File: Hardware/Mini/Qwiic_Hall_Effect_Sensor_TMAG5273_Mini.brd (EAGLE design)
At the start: 25.4 x 12.7 mm, 38 parts, among them J1 Vertical Qwiic Connector, J2 Vertical Qwiic Connector, Q1 20V/4.2A/52mΩ/1.4W, U1 TMAG5273

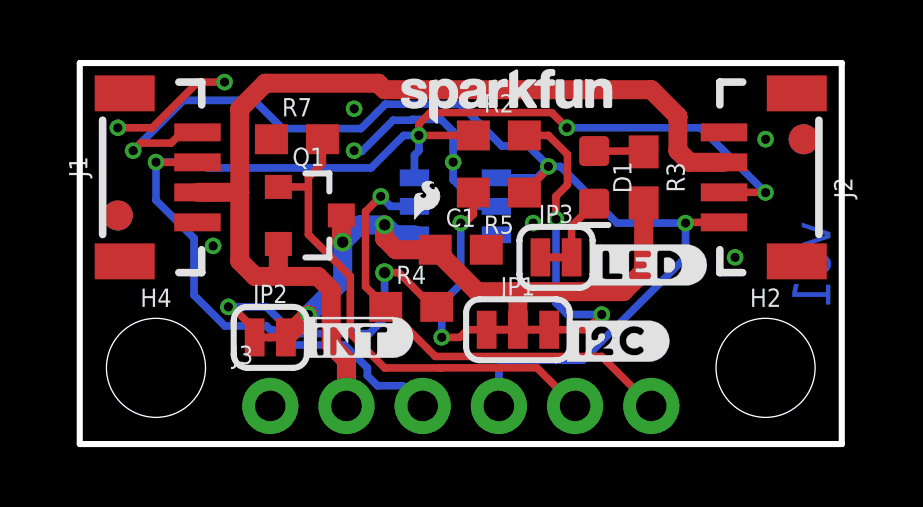
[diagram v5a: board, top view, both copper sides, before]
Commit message: Design review updates
Addition of gerber files for both mini and 1x1, adjusted board for reds engineering checklist run.
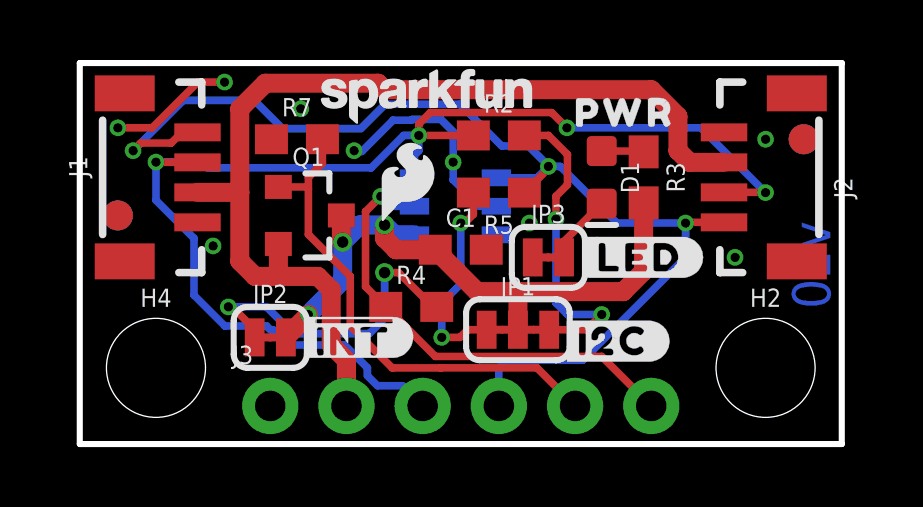
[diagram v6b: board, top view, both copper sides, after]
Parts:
- added U$1: (no value), output:PWR5282
- LOGO6: value SFE_LOGO_FLAME0.05_INCH -> SFE_LOGO_FLAME.1_INCH; device SparkFun-Aesthetics:SFE_LOGO_FLAME_.05 -> SparkFun-Aesthetics:SFE_LOGO_FLAME_.1
- moved LOGO4 2.67 mm to (11.6, 11.7)
- moved LOGO6 0.90 mm to (10.9, 8.76)
- moved U$10 0.28 mm to (18.7, 6.22)
- moved D1 0.25 mm to (17.4, 8.89)
- moved JP3 0.25 mm to (15.6, 6.22)
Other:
- board text added: "v10"
- board text removed: "v01"
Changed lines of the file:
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@@
 <layer number="37" name="tTest" color="7" fill="1" visible="no" active="yes"/>
 <layer number="38" name="bTest" color="7" fill="1" visible="no" active="yes"/>
-<layer number="39" name="tKeepout" color="4" fill="11" visible="no" active="yes"/>
-<layer number="40" name="bKeepout" color="1" fill="11" visible="no" active="yes"/>
-<layer number="41" name="tRestrict" color="4" fill="10" visible="no" active="yes"/>
-<layer number="42" name="bRestrict" color="1" fill="10" visible="no" active="yes"/>
+<layer number="39" name="tKeepout" color="4" fill="11" visible="yes" active="yes"/>
+<layer number="40" name="bKeepout" color="1" fill="11" visible="yes" active="yes"/>
+<layer number="41" name="tRestrict" color="4" fill="10" visible="yes" active="yes"/>
+<layer number="42" name="bRestrict" color="1" fill="10" visible="yes" active="yes"/>
 <layer number="43" name="vRestrict" color="2" fill="10" visible="no" active="yes"/>
 <layer number="44" name="Drills" color="7" fill="1" visible="no" active="yes"/>
 <layer number="45" name="Holes" color="7" fill="1" visible="yes" active="yes"/>
-<layer number="46" name="Milling" color="3" fill="1" visible="yes" active="yes"/>
+<layer number="46" name="Milling" color="3" fill="1" visible="no" active="yes"/>
 <layer number="47" name="Measures" color="7" fill="1" visible="no" active="yes"/>
 <layer number="48" name="Document" color="7" fill="1" visible="no" active="yes"/>
@@
 <dimension x1="4.699" y1="8.89" x2="0" y2="8.89" x3="2.3495" y3="19.05" textsize="1.778" layer="47" unit="inch"/>
 <dimension x1="2.54" y1="2.54" x2="0" y2="2.54" x3="1.27" y3="22.86" textsize="1.778" layer="47" unit="inch"/>
-<text x="24.384" y="5.969" size="1.27" layer="16" font="vector" ratio="15" rot="SMR270" align="center">v01</text>
+<text x="24.384" y="5.969" size="1.27" layer="16" font="vector" ratio="15" rot="SMR270" align="center">v10</text>
 </plain>
 <attributes>
@@
 <element name="FRAME1" library="SparkFun-Aesthetics" package="CREATIVE_COMMONS" value="FRAME-LETTER" x="-11.43" y="-24.13" smashed="yes">
 <attribute name="DESIGNER" value="M. Chodikov" x="68.58" y="-78.74" size="1.778" layer="27" display="off"/>
-<attribute name="REV" value="v01" x="68.58" y="-78.74" size="1.778" layer="27" display="off"/>
+<attribute name="REV" value="v10" x="68.58" y="-78.74" size="1.778" layer="27" display="off"/>
 </element>
 <element name="H2" library="SparkFun-Hardware" package="STAND-OFF" value="STAND-OFF" x="22.86" y="2.54" smashed="yes">
@@
 <attribute name="VALUE" x="6.35" y="2.413" size="0.6096" layer="27" font="vector" ratio="20" align="top-center"/>
 </element>
-<element name="JP3" library="SparkFun-Jumpers" package="SMT-JUMPER_2_NC_TRACE_SILK" package3d_urn="urn:adsk.eagle:package:39281/1" value="JUMPER-SMT_2_NC_TRACE_SILK" x="15.875" y="6.223" smashed="yes">
-<attribute name="NAME" x="15.875" y="7.366" size="0.6096" layer="25" font="vector" ratio="20" align="bottom-center"/>
-<attribute name="VALUE" x="15.875" y="5.08" size="0.6096" layer="27" font="vector" ratio="20" align="top-center"/>
+<element name="JP3" library="SparkFun-Jumpers" package="SMT-JUMPER_2_NC_TRACE_SILK" package3d_urn="urn:adsk.eagle:package:39281/1" value="JUMPER-SMT_2_NC_TRACE_SILK" x="15.621" y="6.223" smashed="yes">
+<attribute name="NAME" x="15.621" y="7.366" size="0.6096" layer="25" font="vector" ratio="20" align="bottom-center"/>
+<attribute name="VALUE" x="15.621" y="5.08" size="0.6096" layer="27" font="vector" ratio="20" align="top-center"/>
 </element>
 <element name="LOGO1" library="SparkFun-Aesthetics" package="OSHW-LOGO-MINI" value="OSHW-LOGOMINI" x="2.54" y="6.35" smashed="yes" rot="MR0"/>
 <element name="LOGO2" library="SparkFun-Aesthetics" package="SFE_LOGO_NAME_FLAME_5MM" value="SFE_LOGO_NAME_FLAME5_MM" x="6.35" y="8.89" smashed="yes" rot="MR0"/>
 <element name="LOGO3" library="SparkFun-Aesthetics" package="QWIIC_4MM" value="QWIIC_LOGO_4MM" x="22.86" y="7.366" smashed="yes" rot="MR0"/>
-<element name="LOGO4" library="SparkFun-Aesthetics" package="SFE_LOGO_NAME_7MM" value="SFE_LOGO_NAME7_MM" x="14.224" y="11.684" smashed="yes"/>
+<element name="LOGO4" library="SparkFun-Aesthetics" package="SFE_LOGO_NAME_7MM" value="SFE_LOGO_NAME7_MM" x="11.557" y="11.684" smashed="yes"/>
 <element name="LOGO5" library="SparkFun-Aesthetics" package="ORDERING_INSTRUCTIONS" value="SPECIAL_INSTRUCTIONS-ORDERING" x="44.45" y="50.8" smashed="yes"/>
-<element name="LOGO6" library="SparkFun-Aesthetics" package="SFE_LOGO_FLAME_.05" value="SFE_LOGO_FLAME0.05_INCH" x="11.557" y="8.128" smashed="yes"/>
+<element name="LOGO6" library="SparkFun-Aesthetics" package="SFE_LOGO_FLAME_.1" value="SFE_LOGO_FLAME.1_INCH" x="10.922" y="8.763" smashed="yes"/>
 <element name="R2" library="SparkFun-Resistors" package="0603" value="2.2k" x="13.97" y="10.287" smashed="yes">
 <attribute name="NAME" x="13.97" y="11.049" size="0.6096" layer="25" font="vector" ratio="20" align="bottom-center"/>
@@
 <attribute name="VALUE" x="5.08" y="-0.762" size="0.6096" layer="27" font="vector" ratio="20"/>
 </element>
-<element name="U$10" library="output" package="#LED#5275" value="" x="18.796" y="5.969" smashed="yes"/>
-<element name="D1" library="SparkFun-LED" package="LED-0603" value="Red" x="17.145" y="8.89" smashed="yes" rot="R270">
-<attribute name="NAME" x="17.78" y="8.89" size="0.6096" layer="25" font="vector" ratio="20" rot="R270" align="bottom-center"/>
-<attribute name="PROD_ID" value="DIO-17976" x="17.145" y="8.89" size="1.778" layer="27" font="vector" rot="R270" display="off"/>
-<attribute name="VALUE" x="16.51" y="8.89" size="0.6096" layer="27" font="vector" ratio="20" rot="R270" align="top-center"/>
+<element name="U$10" library="output" package="#LED#5275" value="" x="18.669" y="6.223" smashed="yes"/>
+<element name="D1" library="SparkFun-LED" package="LED-0603" value="Red" x="17.399" y="8.89" smashed="yes" rot="R270">
+<attribute name="NAME" x="18.034" y="8.89" size="0.6096" layer="25" font="vector" ratio="20" rot="R270" align="bottom-center"/>
+<attribute name="PROD_ID" value="DIO-17976" x="17.399" y="8.89" size="1.778" layer="27" font="vector" rot="R270" display="off"/>
+<attribute name="VALUE" x="16.764" y="8.89" size="0.6096" layer="27" font="vector" ratio="20" rot="R270" align="top-center"/>
 </element>
 <element name="R3" library="SparkFun-Resistors" package="0603" value="4.7k" x="18.796" y="8.89" smashed="yes" rot="R270">
@@
 </element>
 <element name="U$9" library="output" package="#DISABLE#5279" value="" x="16.51" y="5.461" smashed="yes" rot="MR270"/>
+<element name="U$1" library="output" package="PWR5282" value="" x="18.161" y="11.049" smashed="yes"/>
 </elements>
 <signals>
@@
 <vertex x="25.4" y="0"/>
 </polygon>
-<via x="15.113" y="7.366" extent="1-16" drill="0.3048"/>
+<via x="14.986" y="7.366" extent="1-16" drill="0.3048"/>
 <via x="22.86" y="10.16" extent="1-16" drill="0.3048"/>
 <via x="1.27" y="10.541" extent="1-16" drill="0.3048"/>
 <via x="4.445" y="6.604" extent="1-16" drill="0.3048"/>
 <via x="4.826" y="12.065" extent="1-16" drill="0.3048"/>
-<via x="9.144" y="11.176" extent="1-16" drill="0.3048"/>
+<via x="7.366" y="11.176" extent="1-16" drill="0.3048"/>
 <via x="12.446" y="9.398" extent="1-16" drill="0.3048"/>
 <wire x1="1.27" y1="10.541" x2="2.413" y2="10.541" width="0.254" layer="1"/>
@@
 <contactref element="D1" pad="A"/>
 <contactref element="R3" pad="1"/>
-<wire x1="17.145" y1="9.767" x2="18.769" y2="9.767" width="0.254" layer="1"/>
+<wire x1="17.399" y1="9.767" x2="18.769" y2="9.767" width="0.254" layer="1"/>
 <wire x1="18.769" y1="9.767" x2="18.796" y2="9.74" width="0.254" layer="1"/>
 </signal>
 <signal name="N$1">
 <contactref element="JP3" pad="2"/>
-<wire x1="16.3957" y1="6.223" x2="16.3957" y2="7.2637" width="0.254" layer="1"/>
+<wire x1="16.1417" y1="6.223" x2="16.1417" y2="6.7557" width="0.254" layer="1"/>
 <contactref element="D1" pad="C"/>
-<wire x1="16.3957" y1="7.2637" x2="17.145" y2="8.013" width="0.254" layer="1"/>
+<wire x1="16.1417" y1="6.7557" x2="17.399" y2="8.013" width="0.254" layer="1"/>
 </signal>
 <signal name="N$5">
@@
 <wire x1="12.0352125" y1="2.537" x2="12.0382125" y2="2.54" width="0.254" layer="1"/>
 <wire x1="15.24" y1="2.54" x2="12.0382125" y2="2.54" width="0.254" layer="1"/>
-<wire x1="10.163" y1="2.537" x2="9.017" y2="3.683" width="0.254" layer="1"/>
-<wire x1="10.163" y1="2.537" x2="12.0352125" y2="2.537" width="0.254" layer="1"/>
-<wire x1="9.017" y1="3.683" x2="9.017" y2="5.588" width="0.254" layer="1"/>
+<wire x1="10.417" y1="2.537" x2="9.017" y2="3.937" width="0.254" layer="1"/>
+<wire x1="10.417" y1="2.537" x2="12.0352125" y2="2.537" width="0.254" layer="1"/>
+<wire x1="9.017" y1="3.937" x2="9.017" y2="5.588" width="0.254" layer="1"/>
 <wire x1="9.017" y1="5.588" x2="7.62" y2="6.985" width="0.254" layer="1"/>
 <wire x1="7.62" y1="6.985" x2="7.62" y2="8.509" width="0.254" layer="1"/>
@@
 </signals>
 <mfgpreviewcolors>
-<mfgpreviewcolor name="soldermaskcolor" color="0xC8000000"/>
+<mfgpreviewcolor name="soldermaskcolor" color="0xC8FF0000"/>
 <mfgpreviewcolor name="silkscreencolor" color="0xFFFFFFFF"/>
 <mfgpreviewcolor name="backgroundcolor" color="0xFF282828"/>

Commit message: Updates from design review
Adjusted traces for better GND connections; changed direction of tail end for the DISABLE pin; changed jumper names in schematic to match layout; added more GND vias to the Mini; updated trace widths to be the correct size
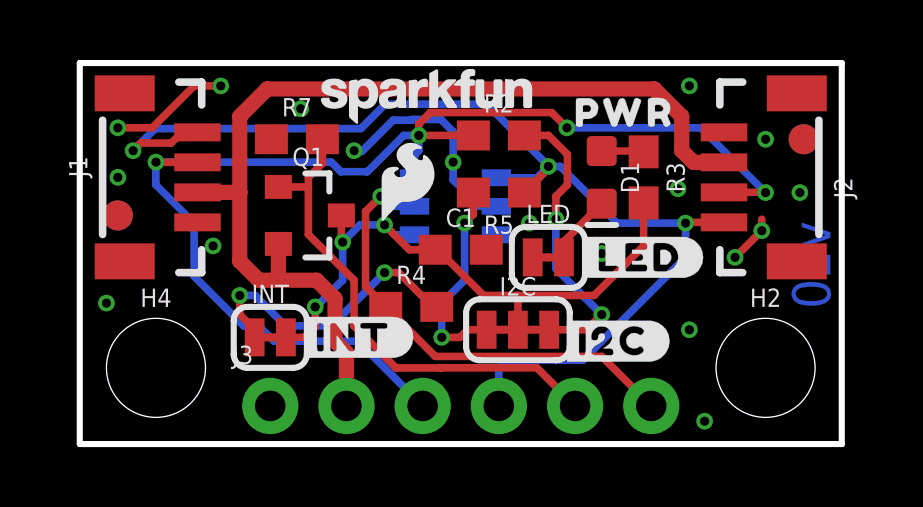
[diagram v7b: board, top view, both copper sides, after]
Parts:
- removed U$15: (no value), output:##INT#5276
- added U$12: (no value), output:#INT#5287
- U$7: device output:##INT#5275 -> output:#DISABLE#5291
- U$9: device output:#DISABLE#5279 -> output:#INT#5285
- moved U$7 7.61 mm to (16.5, 5.46), flipped to the bottom, turned to 270 degrees
- moved U$9 3.10 mm to (19.1, 3.68)
- moved LOGO3 2.16 mm to (22.9, 5.21)
- renumbered JP1 to I2C, JP2 to INT, JP3 to LED
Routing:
- net GND: track 11.5 -> 13.0 mm, vias 9 -> 18
- net N$5: track 11.0 -> 9.80 mm
- net SCL: track 38.4 -> 37.7 mm
- net N$2: track 10.5 -> 9.79 mm

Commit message: Files for ordering
Re-added the correct panel files for the project along with ordering instructions. Made final adjustments from design review and board is ready for order!
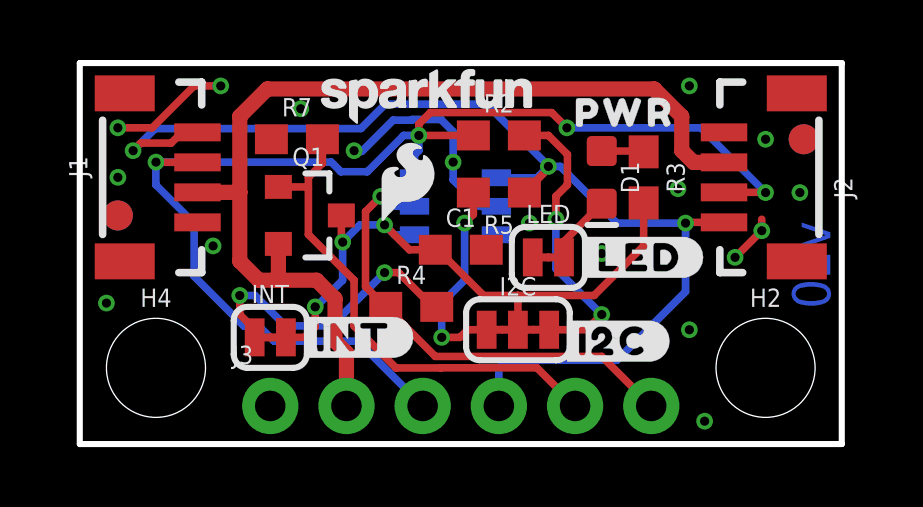
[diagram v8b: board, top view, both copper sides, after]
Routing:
- net SCL: track 37.7 -> 38.3 mm
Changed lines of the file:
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@@
 <drawing>
 <settings>
-<setting alwaysvectorfont="yes"/>
+<setting alwaysvectorfont="no"/>
 <setting verticaltext="up"/>
 </settings>
@@
 <layer number="49" name="Reference" color="7" fill="1" visible="no" active="yes"/>
 <layer number="50" name="dxf" color="7" fill="1" visible="no" active="no"/>
-<layer number="51" name="tDocu" color="6" fill="1" visible="no" active="yes"/>
+<layer number="51" name="tDocu" color="6" fill="1" visible="yes" active="yes"/>
 <layer number="52" name="bDocu" color="7" fill="1" visible="no" active="yes"/>
 <layer number="53" name="tGND_GNDA" color="7" fill="9" visible="no" active="no"/>
@@
 <wire x1="10.1854" y1="11.3284" x2="9.3726" y2="10.5156" width="0.254" layer="16"/>
 <contactref element="J3" pad="4"/>
-<wire x1="16.764" y1="2.794" x2="14.224" y2="2.794" width="0.254" layer="16"/>
+<wire x1="17.907" y1="2.794" x2="14.224" y2="2.794" width="0.254" layer="16"/>
 <wire x1="14.224" y1="2.794" x2="13.97" y2="2.54" width="0.254" layer="16"/>
 <wire x1="13.97" y1="2.54" x2="13.97" y2="1.27" width="0.254" layer="16"/>
-<wire x1="20.193" y1="7.366" x2="20.193" y2="6.223" width="0.254" layer="16"/>
-<wire x1="20.193" y1="6.223" x2="16.764" y2="2.794" width="0.254" layer="16"/>
+<wire x1="20.193" y1="7.366" x2="20.193" y2="5.08" width="0.254" layer="16"/>
+<wire x1="20.193" y1="5.08" x2="17.907" y2="2.794" width="0.254" layer="16"/>
 <wire x1="13.88745" y1="8.8748" x2="15.2422" y2="8.8748" width="0.254" layer="16"/>
 <wire x1="15.2422" y1="8.8748" x2="15.621" y2="9.2536" width="0.254" layer="16"/>
